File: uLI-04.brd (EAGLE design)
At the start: 57 x 38.5 mm, 39 parts, among them IC1 PIC18F14K50-I/SS, IC2 ADM2483, IC3 MCP130T, IC4 78L05F, J1 PICPROG2-V, J5 WEBP6, J6 WEBP6, J7 WEBP6, Q1 12.00 MHz, T1 IRF7306, X1 MINI-USB_SHIELD4P-USB-SPEC, X2 ARK1550/2_S

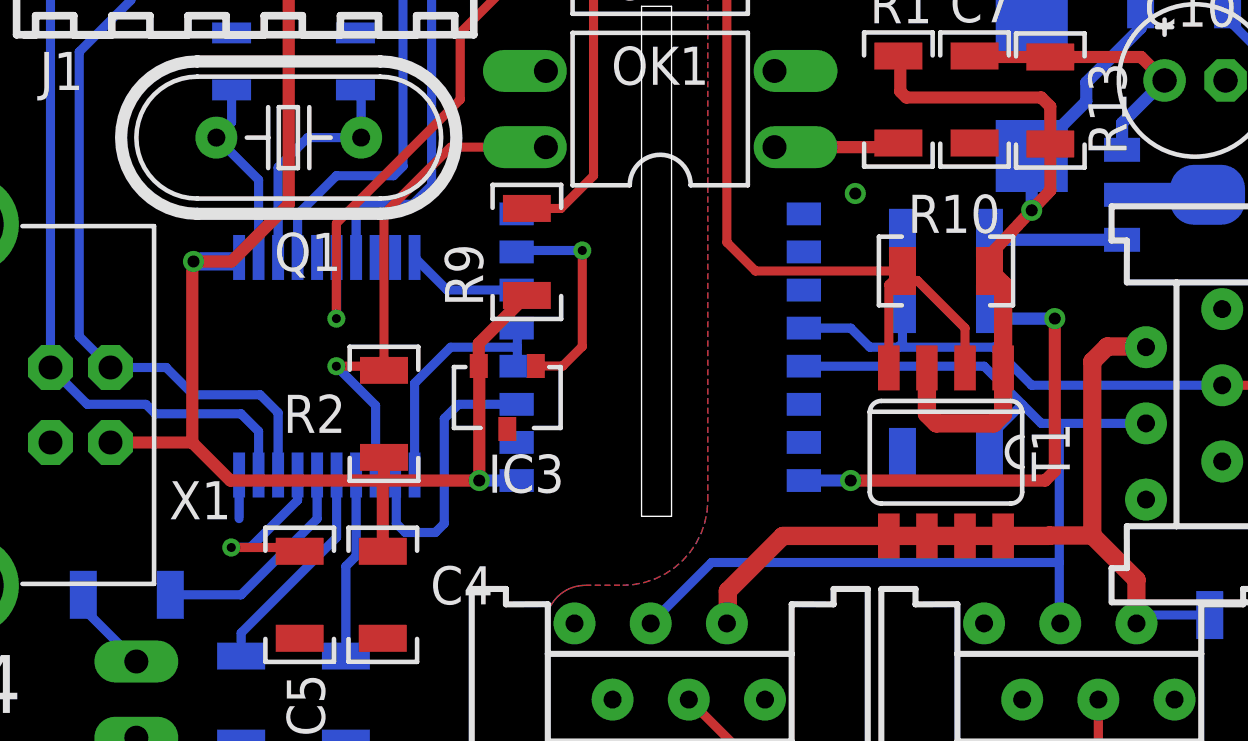
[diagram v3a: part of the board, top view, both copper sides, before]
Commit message: Velikost vnejsiho okraje prokovu -> 0.9 mm.
Close #4.
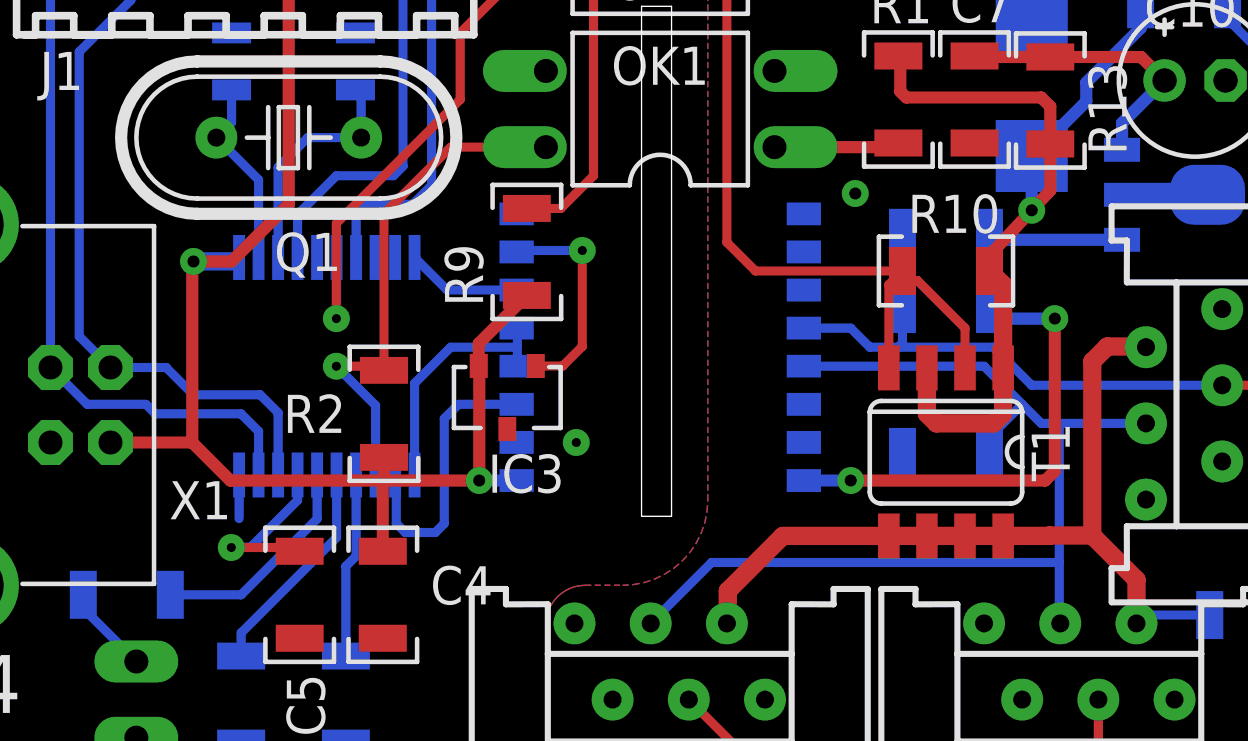
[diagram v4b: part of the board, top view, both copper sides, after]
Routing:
- net GND: vias 0 -> 1
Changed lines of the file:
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@@
 <contactref element="IC2" pad="2"/>
 <contactref element="IC3" pad="3"/>
+<via x="28" y="20" extent="1-16" drill="0.3" diameter="0.9"/>
 </signal>
 <signal name="VBUS">
@@
 <wire x1="18.71" y1="18.9175" x2="18.71" y2="18.075" width="0.3048" layer="16"/>
 <wire x1="18.71" y1="18.075" x2="17.145" y2="16.51" width="0.3048" layer="16"/>
-<via x="16.5" y="16.5" extent="1-16" drill="0.3"/>
+<via x="16.5" y="16.5" extent="1-16" drill="0.3" diameter="0.9"/>
 <wire x1="16.5" y1="16.5" x2="18.6525" y2="16.5" width="0.3048" layer="1"/>
 <wire x1="18.6525" y1="16.5" x2="18.78" y2="16.3725" width="0.3048" layer="1"/>
@@
 <contactref element="C4" pad="1"/>
 <contactref element="R2" pad="2"/>
-<via x="15.24" y="26.035" extent="1-16" drill="0.4"/>
+<via x="15.24" y="26.035" extent="1-16" drill="0.4" diameter="0.9"/>
 <wire x1="18.415" y1="27.94" x2="16.51" y2="26.035" width="0.4064" layer="1"/>
 <wire x1="16.51" y1="26.035" x2="15.24" y2="26.035" width="0.4064" layer="1"/>
@@
 <wire x1="16.6275" y1="26.035" x2="15.24" y2="26.035" width="0.6096" layer="16"/>
 <wire x1="26.0096" y1="18.7325" x2="24.765" y2="18.7325" width="0.4064" layer="16"/>
-<via x="24.765" y="18.7325" extent="1-16" drill="0.4"/>
+<via x="24.765" y="18.7325" extent="1-16" drill="0.4" diameter="0.9"/>
 <wire x1="24.765" y1="18.7325" x2="21.59" y2="18.7325" width="0.4064" layer="1"/>
 <wire x1="21.59" y1="18.7325" x2="21.55" y2="18.7325" width="0.4064" layer="1"/>
@@
 <contactref element="J7" pad="2"/>
 <contactref element="J5" pad="2"/>
-<via x="37.3" y="28.3" extent="1-16" drill="0.4"/>
+<via x="37.3" y="28.3" extent="1-16" drill="0.4" diameter="0.9"/>
 </signal>
 <signal name="VCCINT" class="1">
@@
 <wire x1="41.7725" y1="26.9875" x2="41.7725" y2="24.4475" width="0.4064" layer="16"/>
 <wire x1="35.5854" y1="18.7325" x2="37.1475" y2="18.7325" width="0.4064" layer="16"/>
-<via x="37.1475" y="18.7325" extent="1-16" drill="0.4"/>
+<via x="37.1475" y="18.7325" extent="1-16" drill="0.4" diameter="0.9"/>
 <wire x1="37.1475" y1="18.7325" x2="43.6325" y2="18.7325" width="0.4064" layer="1"/>
 <wire x1="43.6325" y1="18.7325" x2="43.95" y2="19.05" width="0.4064" layer="1"/>
 <wire x1="43.95" y1="19.05" x2="43.95" y2="24.13" width="0.4064" layer="1"/>
-<via x="43.95" y="24.13" extent="1-16" drill="0.4"/>
+<via x="43.95" y="24.13" extent="1-16" drill="0.4" diameter="0.9"/>
 <wire x1="43.95" y1="24.13" x2="42.09" y2="24.13" width="0.4064" layer="16"/>
 <wire x1="42.09" y1="24.13" x2="41.7725" y2="24.4475" width="0.4064" layer="16"/>
@@
 <contactref element="R13" pad="2"/>
 <wire x1="43.18" y1="29.55" x2="43.18" y2="27.74" width="0.4064" layer="16"/>
-<via x="43.18" y="27.74" extent="1-16" drill="0.4"/>
+<via x="43.18" y="27.74" extent="1-16" drill="0.4" diameter="0.9"/>
 <wire x1="43.18" y1="27.74" x2="41.7725" y2="26.2325" width="0.4064" layer="1"/>
 <wire x1="43.8" y1="29.95" x2="43.8" y2="28.4" width="0.4064" layer="1"/>
@@
 <wire x1="26.9875" y1="29.845" x2="23.8125" y2="29.845" width="0.3048" layer="1"/>
 <wire x1="23.8125" y1="29.845" x2="21.59" y2="27.6225" width="0.3048" layer="1"/>
-<via x="20.0025" y="22.5425" extent="1-16" drill="0.3"/>
+<via x="20.0025" y="22.5425" extent="1-16" drill="0.3" diameter="0.9"/>
 <wire x1="21.31" y1="18.9175" x2="21.31" y2="21.235" width="0.3048" layer="16"/>
 <wire x1="21.31" y1="21.235" x2="20.0025" y2="22.5425" width="0.3048" layer="16"/>
@@
 <wire x1="20.01" y1="26.1675" x2="20.01" y2="24.1375" width="0.3048" layer="16"/>
 <wire x1="20.01" y1="24.1375" x2="20.0025" y2="24.13" width="0.3048" layer="16"/>
-<via x="20.0025" y="24.13" extent="1-16" drill="0.3"/>
+<via x="20.0025" y="24.13" extent="1-16" drill="0.3" diameter="0.9"/>
 <wire x1="20.0025" y1="24.13" x2="20.0025" y2="27.305" width="0.3048" layer="1"/>
 <wire x1="20.0025" y1="27.305" x2="24.13" y2="31.4325" width="0.3048" layer="1"/>
@@
 <signal name="PV">
 <contactref element="IC2" pad="7"/>
-<via x="28.2" y="26.4" extent="1-16" drill="0.3"/>
+<via x="28.2" y="26.4" extent="1-16" drill="0.3" diameter="0.9"/>
 <wire x1="28.2" y1="26.4" x2="26.0571" y2="26.4" width="0.3048" layer="16"/>
 <wire x1="26.0571" y1="26.4" x2="26.0096" y2="26.3525" width="0.3048" layer="16"/>

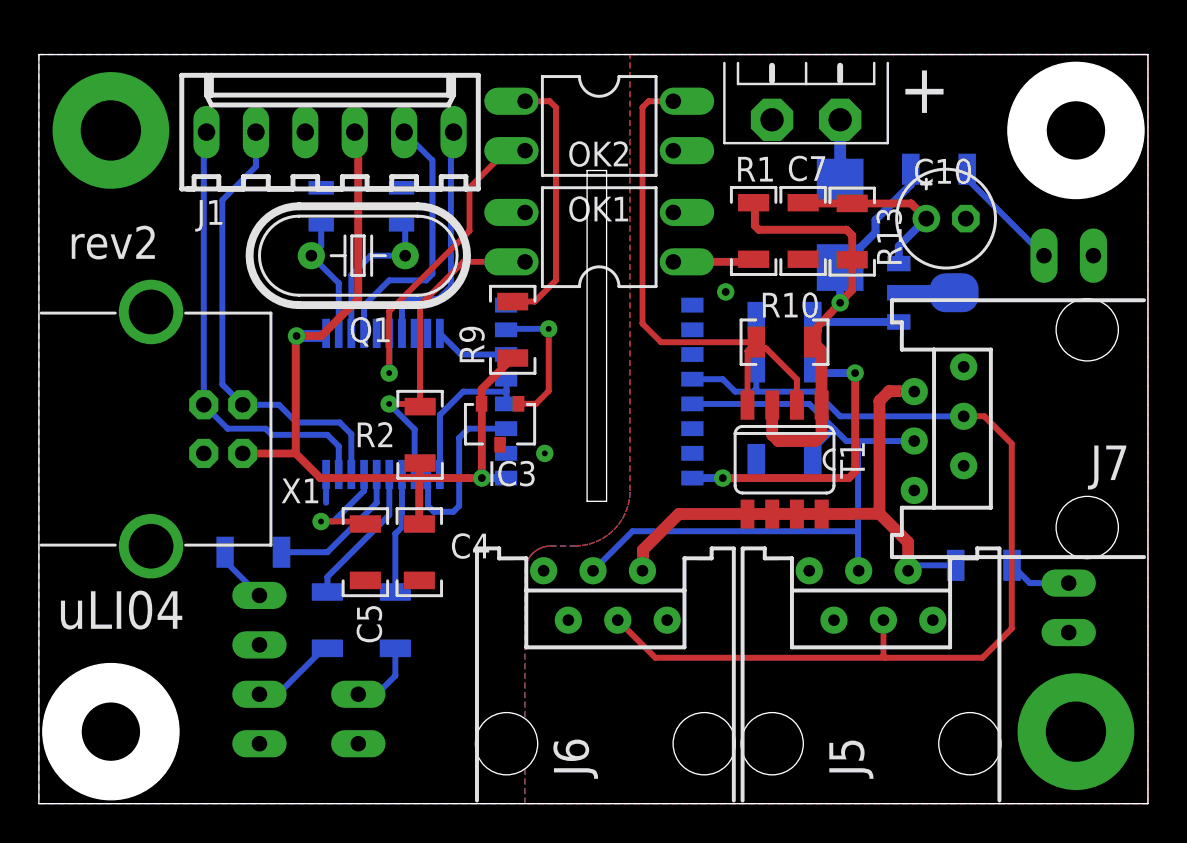
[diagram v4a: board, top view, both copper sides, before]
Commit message: Drobne zmeny.
* Upraveno DRC na bezpecnejsi mezery.
* Prokovy nastaveny globalne na 0.4 mm.
* Posunuta dioda S2M.
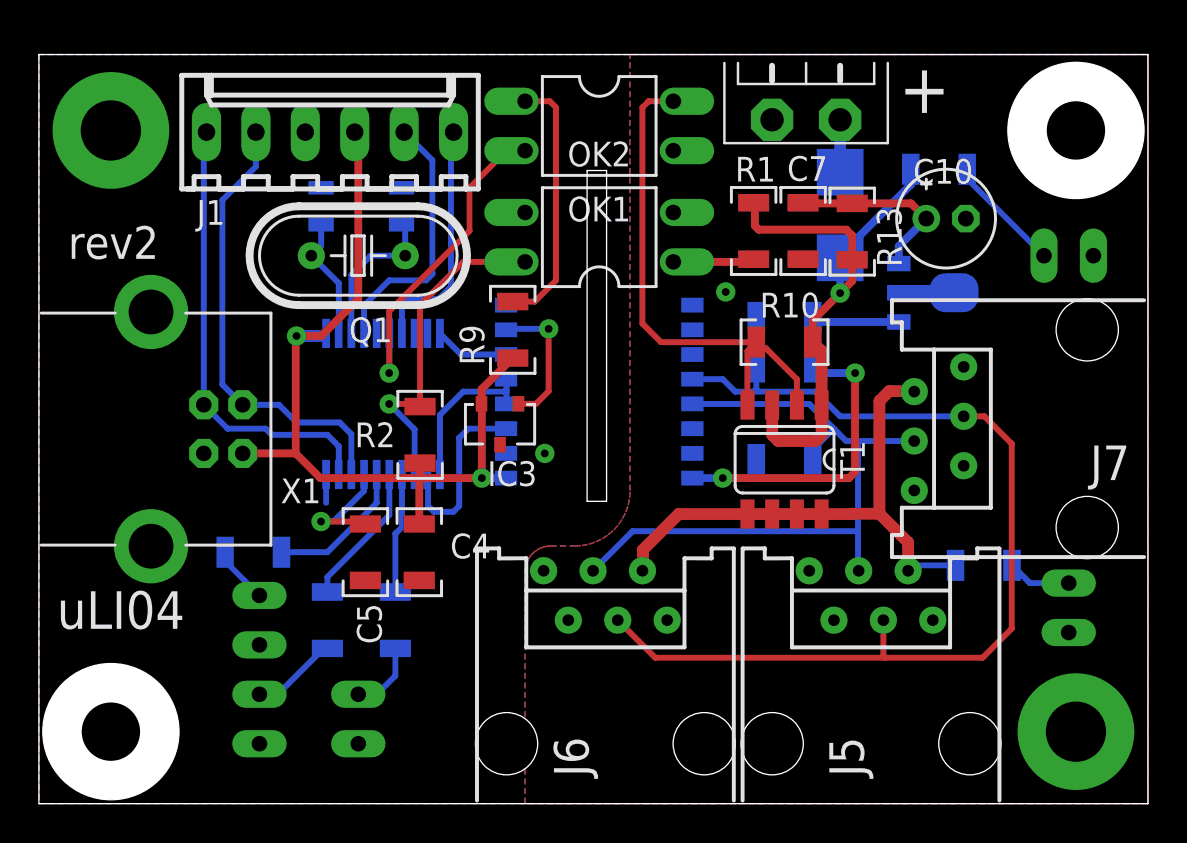
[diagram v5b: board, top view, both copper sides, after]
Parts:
- moved D2 0.50 mm to (43.2, 32.2)
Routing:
- net +NAP2: track 3.20 -> 2.70 mm
